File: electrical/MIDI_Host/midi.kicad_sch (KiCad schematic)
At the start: 25 parts, among them U10 BL1551B, U11 6N137, U12 6N137, U13 74HC1G14GV, U14 BL1551B, U9 BL1551B

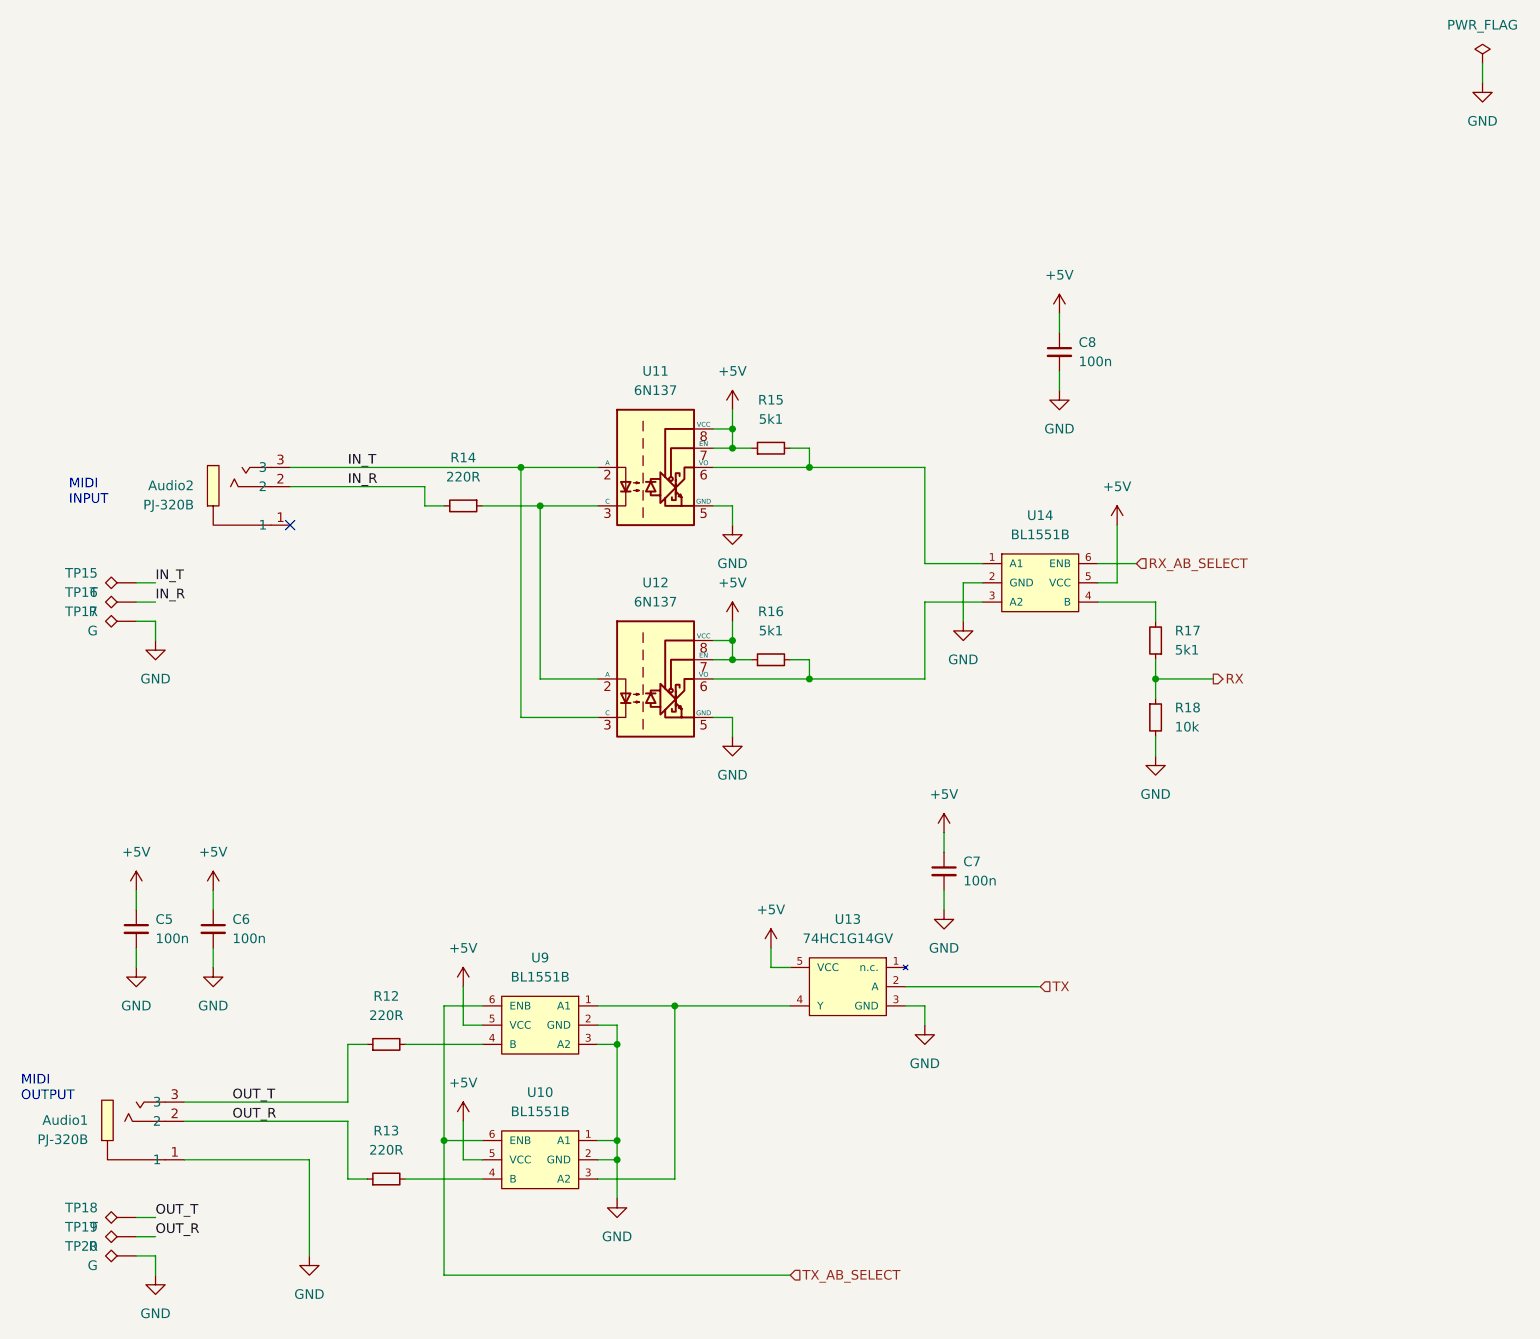
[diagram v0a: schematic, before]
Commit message: SUKU v3 laout finished, decoupling and esd protection improved
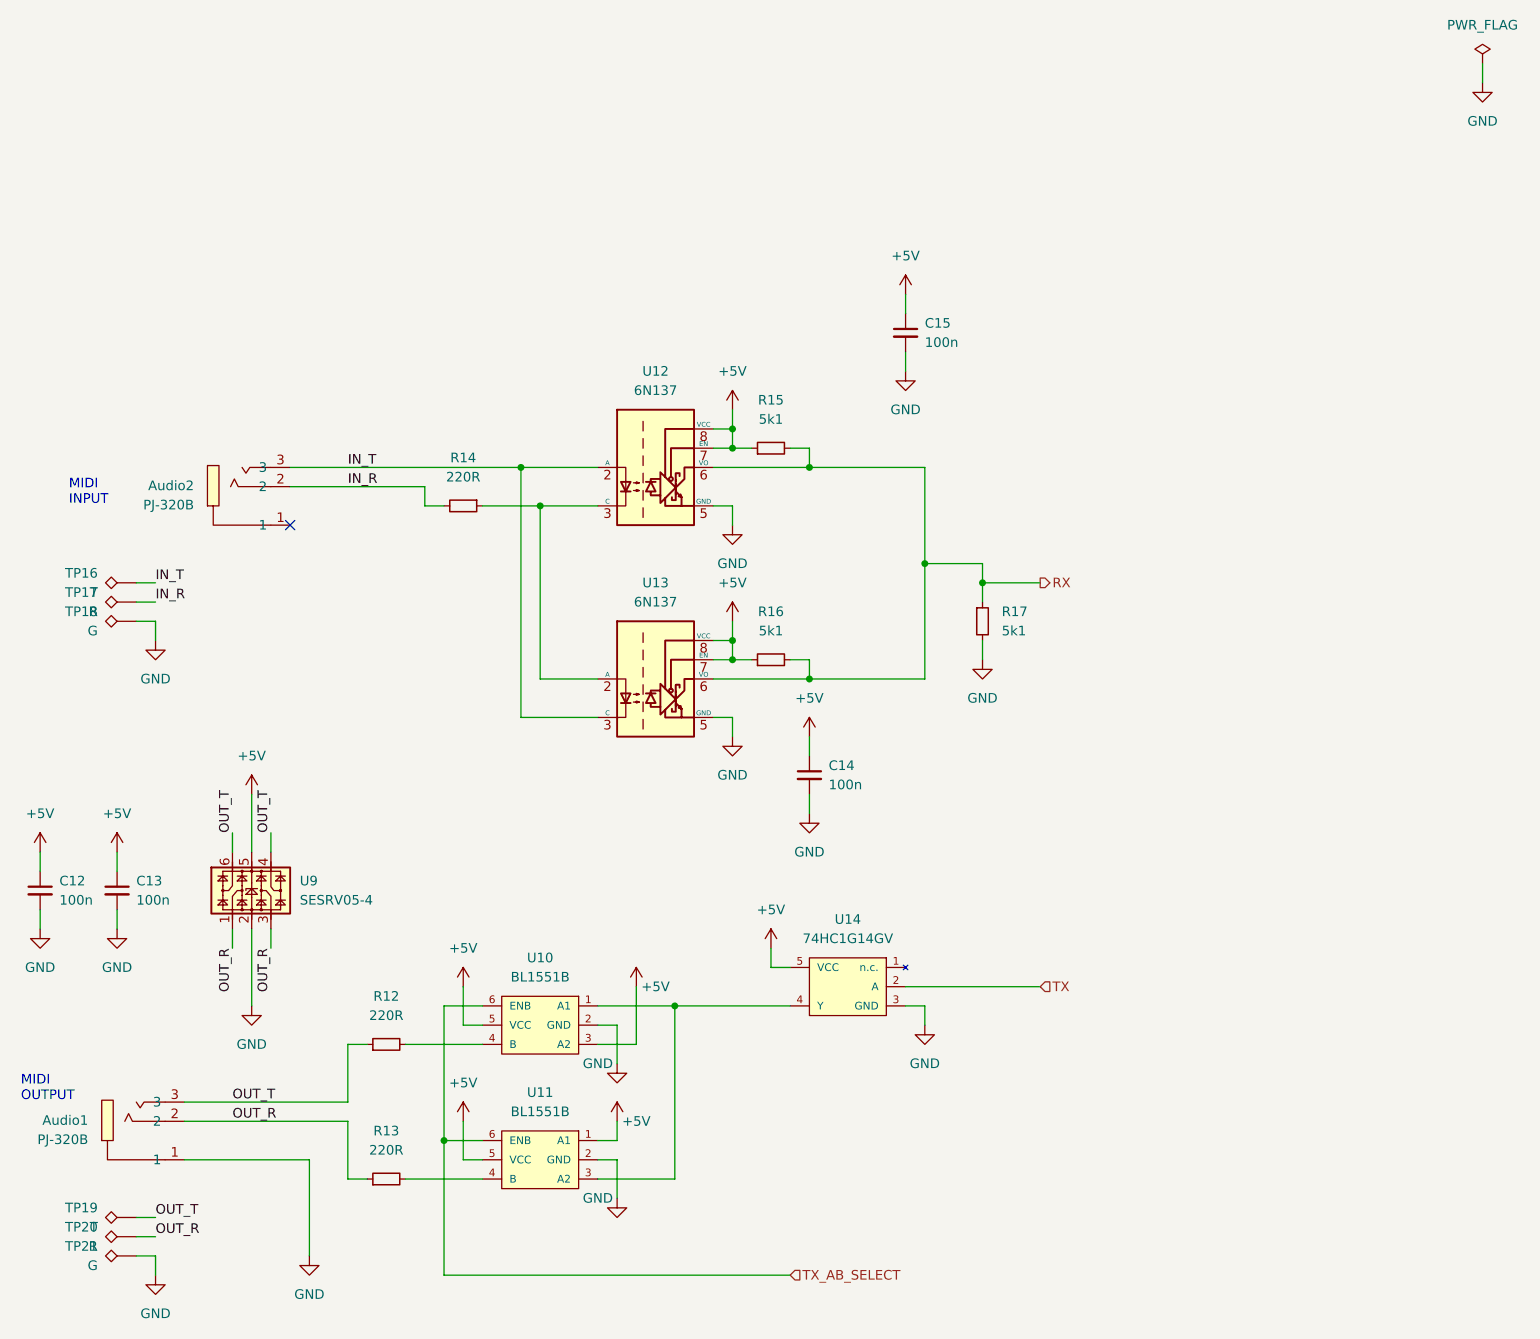
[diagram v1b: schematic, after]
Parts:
- removed R17: 5k1, suku_basics:RES_0805, symbol suku_basics:RES
- removed U14: BL1551B, suku_basics:SOT-363_SC-70-6, symbol suku_basics:BL1551B
- added U9: SESRV05-4, suku_basics:SOT-23-6, symbol suku_basics:U_ESD_4ch
- C12: renamed from C5; footprint suku_basics:CAP_0805 -> suku_basics:CAP_0402
- C13: renamed from C6; footprint suku_basics:CAP_0805 -> suku_basics:CAP_0402
- C14: renamed from C8; footprint suku_basics:CAP_0805 -> suku_basics:CAP_0402
- C15: renamed from C7; footprint suku_basics:CAP_0805 -> suku_basics:CAP_0402
- R12, R13, R14, R15, R16: footprint suku_basics:RES_0805 -> suku_basics:RES_0402
- R17: renamed from R18; value 10k -> 5k1; footprint suku_basics:RES_0805 -> suku_basics:RES_0402
- renumbered TP15 to TP16, TP16 to TP17, TP17 to TP18, TP18 to TP19, TP19 to TP20, TP20 to TP21, U9 to U10, U10 to U11, U11 to U12, U12 to U13, U13 to U14
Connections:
- net +5V: now also U10.3 (A2), U11.1 (A1), U9.5
- net GND: now also U9.2; no longer U10.3 (A2), U11.1 (A1)
- net OUT_R: now also U9.1, U9.3
- net OUT_T: now also U9.4, U9.6
- net RX: now also R15.2, R16.2, U12.6 (VO), U13.6 (VO)
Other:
- moved on the sheet: C12, C13, C14, C15, R17

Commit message: SUKU bootloader updated
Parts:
- renumbered C12 to C13, C13 to C14, C14 to C15, C15 to C16, R12 to R13, R13 to R14, R14 to R15, R15 to R16, R16 to R17, R17 to R18
